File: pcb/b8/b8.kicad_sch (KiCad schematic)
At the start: 29 parts, among them J1 USB, J2 ISP Programming, SW1 SW_Push, SW2 SW_Push, SW3 SW_Push, SW4 SW_Push, SW5 SW_Push, SW6 SW_Push, SW7 SW_Push, SW8 SW_Push, U1 ATtiny4313-P, Y1 20MHz

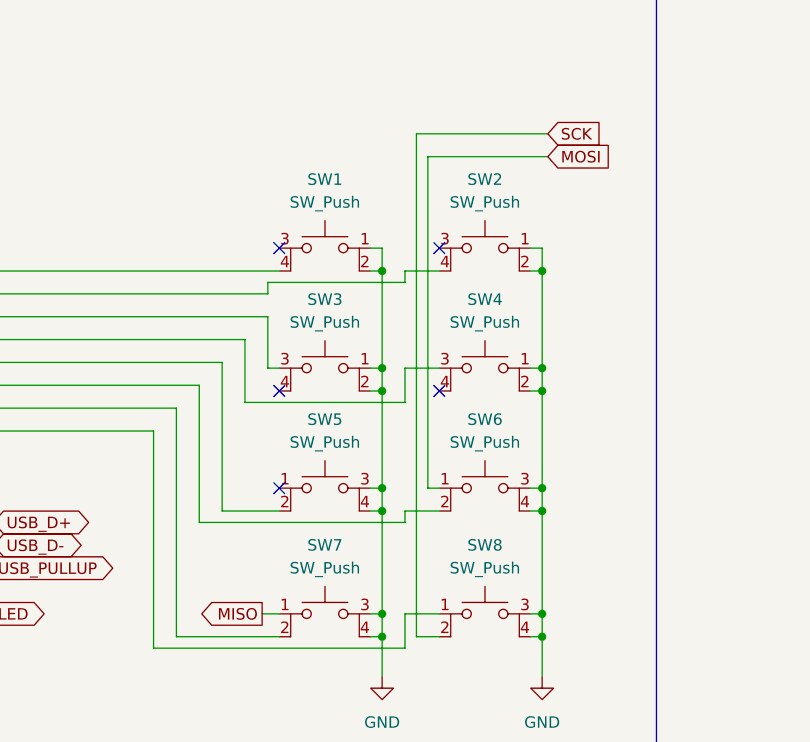
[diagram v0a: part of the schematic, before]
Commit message: pcb: b8: revision 20240403
some minor pcb fixes. this also moves the pcb files to pcb/b8, preparing
to introduce other pcb variants. this also moves the kicad library to
pcb/lib and adds the missing LICENSE file.
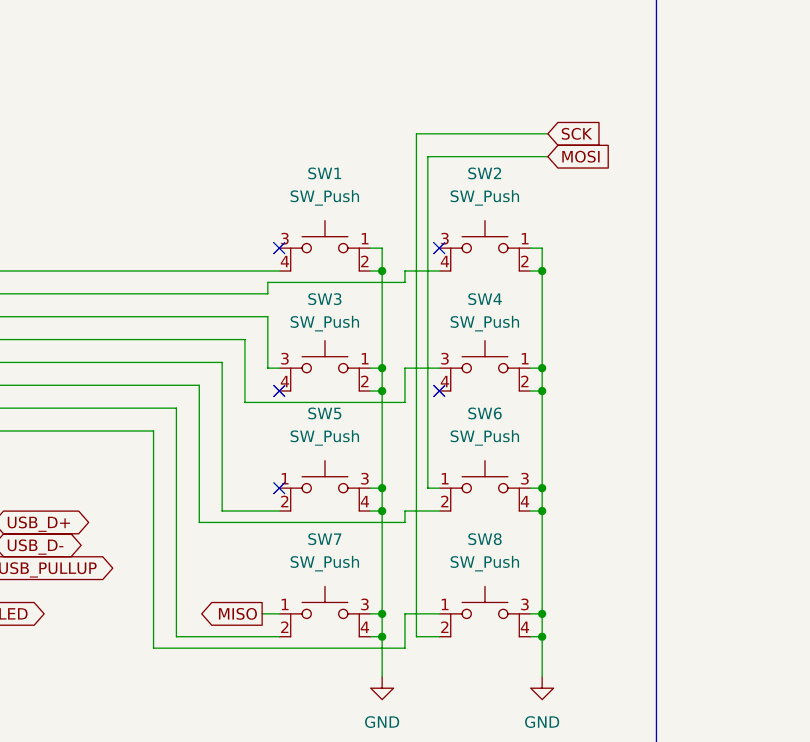
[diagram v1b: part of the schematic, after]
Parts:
- C3: footprint Capacitor_THT:C_Disc_D4.3mm_W1.9mm_P5.00mm -> b8:C_TDK_FA28
- C4: footprint custom:CP_Radial_D5.0mm_P2.50mm_Horizontal -> b8:CP_Radial_D5.0mm_P2.50mm_Horizontal
- J1: footprint custom:RND_205-00862 -> b8:USB_Mini-B_PTH
- R1, R2, R3, R4: footprint Resistor_THT:R_Axial_DIN0207_L6.3mm_D2.5mm_P10.16mm_Horizontal -> b8:R_YAGEO_MFR-25FTE52_Horizontal
- SW1, SW2, SW3, SW4, SW5, SW6, SW7, SW8: footprint custom:SW_PUSH-12mm -> b8:SW_PUSH-12mm; symbol custom:SW_Push -> b8:SW_Push
- Y1: footprint Crystal:Crystal_HC49-U_Vertical -> Crystal:Crystal_HC49-4H_Vertical
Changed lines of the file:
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@@
   (title_block
     (title "b8")
-    (date "2022-12-22")
-    (rev "1.1")
+    (date "2024-04-03")
+    (rev "20240403")
     (comment 3 "Released under CERN Open Hardware Licence Version 2 - Strongly Reciprocal")
     (comment 4 "Designed by: Rafael G. Martins")
@@
     )
   )
-  (symbol (lib_id "custom:SW_Push") (at 225.425 71.755 0) (mirror y) (unit 1)
-    (in_bom yes) (on_board yes) (dnp no) (fields_autoplaced)
-    (property "Reference" "SW2" (at 225.425 64.135 0)
-      (effects (font (size 1.27 1.27)))
-    )
-    (property "Value" "SW_Push" (at 225.425 66.675 0)
-      (effects (font (size 1.27 1.27)))
-    )
-    (property "Footprint" "custom:SW_PUSH-12mm" (at 225.425 66.675 0)
+  (symbol (lib_id "b8:SW_Push") (at 225.425 71.755 0) (mirror y) (unit 1)
+    (in_bom yes) (on_board yes) (dnp no) (fields_autoplaced)
+    (property "Reference" "SW2" (at 225.425 63.5 0)
+      (effects (font (size 1.27 1.27)))
+    )
+    (property "Value" "SW_Push" (at 225.425 66.04 0)
+      (effects (font (size 1.27 1.27)))
+    )
+    (property "Footprint" "b8:SW_PUSH-12mm" (at 225.425 66.675 0)
       (effects (font (size 1.27 1.27)) hide)
     )
@@
     )
   )
-  (symbol (lib_id "custom:SW_Push") (at 225.425 98.425 0) (unit 1)
-    (in_bom yes) (on_board yes) (dnp no) (fields_autoplaced)
-    (property "Reference" "SW6" (at 225.425 90.805 0)
-      (effects (font (size 1.27 1.27)))
-    )
-    (property "Value" "SW_Push" (at 225.425 93.345 0)
-      (effects (font (size 1.27 1.27)))
-    )
-    (property "Footprint" "custom:SW_PUSH-12mm" (at 225.425 93.345 0)
+  (symbol (lib_id "b8:SW_Push") (at 225.425 98.425 0) (unit 1)
+    (in_bom yes) (on_board yes) (dnp no) (fields_autoplaced)
+    (property "Reference" "SW6" (at 225.425 90.17 0)
+      (effects (font (size 1.27 1.27)))
+    )
+    (property "Value" "SW_Push" (at 225.425 92.71 0)
+      (effects (font (size 1.27 1.27)))
+    )
+    (property "Footprint" "b8:SW_PUSH-12mm" (at 225.425 93.345 0)
       (effects (font (size 1.27 1.27)) hide)
     )
@@
     )
   )
-  (symbol (lib_id "custom:SW_Push") (at 207.645 85.09 0) (mirror y) (unit 1)
+  (symbol (lib_id "b8:SW_Push") (at 207.645 85.09 0) (mirror y) (unit 1)
     (in_bom yes) (on_board yes) (dnp no) (fields_autoplaced)
     (property "Reference" "SW3" (at 207.645 77.47 0)
@@
       (effects (font (size 1.27 1.27)))
     )
-    (property "Footprint" "custom:SW_PUSH-12mm" (at 207.645 80.01 0)
+    (property "Footprint" "b8:SW_PUSH-12mm" (at 207.645 80.01 0)
       (effects (font (size 1.27 1.27)) hide)
     )
@@
       (effects (font (size 1.27 1.27)))
     )
-    (property "Footprint" "custom:RND_205-00862" (at 66.04 93.98 0)
+    (property "Footprint" "b8:USB_Mini-B_PTH" (at 66.04 93.98 0)
       (effects (font (size 1.27 1.27)) hide)
     )
@@
       (effects (font (size 1.27 1.27)))
     )
-    (property "Footprint" "Resistor_THT:R_Axial_DIN0207_L6.3mm_D2.5mm_P10.16mm_Horizontal" (at 87.63 97.028 90)
+    (property "Footprint" "b8:R_YAGEO_MFR-25FTE52_Horizontal" (at 87.63 97.028 90)
       (effects (font (size 1.27 1.27)) hide)
     )
@@
       (effects (font (size 1.27 1.27)))
     )
-    (property "Footprint" "custom:CP_Radial_D5.0mm_P2.50mm_Horizontal" (at 164.465 59.3598 0)
+    (property "Footprint" "b8:CP_Radial_D5.0mm_P2.50mm_Horizontal" (at 164.465 59.3598 0)
       (effects (font (size 1.27 1.27)) hide)
     )
@@
     )
   )
-  (symbol (lib_id "custom:SW_Push") (at 225.425 112.395 0) (unit 1)
-    (in_bom yes) (on_board yes) (dnp no) (fields_autoplaced)
-    (property "Reference" "SW8" (at 225.425 104.775 0)
-      (effects (font (size 1.27 1.27)))
-    )
-    (property "Value" "SW_Push" (at 225.425 107.315 0)
-      (effects (font (size 1.27 1.27)))
-    )
-    (property "Footprint" "custom:SW_PUSH-12mm" (at 225.425 107.315 0)
+  (symbol (lib_id "b8:SW_Push") (at 225.425 112.395 0) (unit 1)
+    (in_bom yes) (on_board yes) (dnp no) (fields_autoplaced)
+    (property "Reference" "SW8" (at 225.425 104.14 0)
+      (effects (font (size 1.27 1.27)))
+    )
+    (property "Value" "SW_Push" (at 225.425 106.68 0)
+      (effects (font (size 1.27 1.27)))
+    )
+    (property "Footprint" "b8:SW_PUSH-12mm" (at 225.425 107.315 0)
       (effects (font (size 1.27 1.27)) hide)
     )
@@
       (effects (font (size 1.27 1.27)))
     )
-    (property "Footprint" "Resistor_THT:R_Axial_DIN0207_L6.3mm_D2.5mm_P10.16mm_Horizontal" (at 78.105 128.143 90)
+    (property "Footprint" "b8:R_YAGEO_MFR-25FTE52_Horizontal" (at 78.105 128.143 90)
       (effects (font (size 1.27 1.27)) hide)
     )
@@
       (effects (font (size 1.27 1.27)))
     )
-    (property "Footprint" "Resistor_THT:R_Axial_DIN0207_L6.3mm_D2.5mm_P10.16mm_Horizontal" (at 87.63 94.488 90)
+    (property "Footprint" "b8:R_YAGEO_MFR-25FTE52_Horizontal" (at 87.63 94.488 90)
       (effects (font (size 1.27 1.27)) hide)
     )
@@
     )
   )
-  (symbol (lib_id "custom:SW_Push") (at 225.425 85.09 0) (mirror y) (unit 1)
+  (symbol (lib_id "b8:SW_Push") (at 225.425 85.09 0) (mirror y) (unit 1)
     (in_bom yes) (on_board yes) (dnp no) (fields_autoplaced)
     (property "Reference" "SW4" (at 225.425 77.47 0)
@@
       (effects (font (size 1.27 1.27)))
     )
-    (property "Footprint" "custom:SW_PUSH-12mm" (at 225.425 80.01 0)
+    (property "Footprint" "b8:SW_PUSH-12mm" (at 225.425 80.01 0)
       (effects (font (size 1.27 1.27)) hide)
     )
@@
     )
   )
-  (symbol (lib_id "custom:SW_Push") (at 207.645 71.755 0) (mirror y) (unit 1)
-    (in_bom yes) (on_board yes) (dnp no) (fields_autoplaced)
-    (property "Reference" "SW1" (at 207.645 64.135 0)
-      (effects (font (size 1.27 1.27)))
-    )
-    (property "Value" "SW_Push" (at 207.645 66.675 0)
-      (effects (font (size 1.27 1.27)))
-    )
-    (property "Footprint" "custom:SW_PUSH-12mm" (at 207.645 66.675 0)
+  (symbol (lib_id "b8:SW_Push") (at 207.645 71.755 0) (mirror y) (unit 1)
+    (in_bom yes) (on_board yes) (dnp no) (fields_autoplaced)
+    (property "Reference" "SW1" (at 207.645 63.5 0)
+      (effects (font (size 1.27 1.27)))
+    )
+    (property "Value" "SW_Push" (at 207.645 66.04 0)
+      (effects (font (size 1.27 1.27)))
+    )
+    (property "Footprint" "b8:SW_PUSH-12mm" (at 207.645 66.675 0)
       (effects (font (size 1.27 1.27)) hide)
     )
@@
     )
   )
-  (symbol (lib_id "custom:SW_Push") (at 207.645 98.425 0) (unit 1)
-    (in_bom yes) (on_board yes) (dnp no) (fields_autoplaced)
-    (property "Reference" "SW5" (at 207.645 90.805 0)
-      (effects (font (size 1.27 1.27)))
-    )
-    (property "Value" "SW_Push" (at 207.645 93.345 0)
-      (effects (font (size 1.27 1.27)))
-    )
-    (property "Footprint" "custom:SW_PUSH-12mm" (at 207.645 93.345 0)
+  (symbol (lib_id "b8:SW_Push") (at 207.645 98.425 0) (unit 1)
+    (in_bom yes) (on_board yes) (dnp no) (fields_autoplaced)
+    (property "Reference" "SW5" (at 207.645 90.17 0)
+      (effects (font (size 1.27 1.27)))
+    )
+    (property "Value" "SW_Push" (at 207.645 92.71 0)
+      (effects (font (size 1.27 1.27)))
+    )
+    (property "Footprint" "b8:SW_PUSH-12mm" (at 207.645 93.345 0)
       (effects (font (size 1.27 1.27)) hide)
     )
@@
       (effects (font (size 1.27 1.27)))
     )
-    (property "Footprint" "Capacitor_THT:C_Disc_D4.3mm_W1.9mm_P5.00mm" (at 151.765 59.3598 0)
+    (property "Footprint" "b8:C_TDK_FA28" (at 151.765 59.3598 0)
       (effects (font (size 1.27 1.27)) hide)
     )
@@
       (effects (font (size 1.27 1.27)) (justify right))
     )
-    (property "Footprint" "Resistor_THT:R_Axial_DIN0207_L6.3mm_D2.5mm_P10.16mm_Horizontal" (at 80.518 85.09 90)
+    (property "Footprint" "b8:R_YAGEO_MFR-25FTE52_Horizontal" (at 80.518 85.09 90)
       (effects (font (size 1.27 1.27)) hide)
     )
@@
       (effects (font (size 1.27 1.27)) (justify right))
     )
-    (property "Footprint" "Crystal:Crystal_HC49-U_Vertical" (at 126.365 84.455 0)
+    (property "Footprint" "Crystal:Crystal_HC49-4H_Vertical" (at 126.365 84.455 0)
       (effects (font (size 1.27 1.27)) hide)
     )
@@
     )
   )
-  (symbol (lib_id "custom:SW_Push") (at 207.645 112.395 0) (unit 1)
-    (in_bom yes) (on_board yes) (dnp no) (fields_autoplaced)
-    (property "Reference" "SW7" (at 207.645 104.775 0)
-      (effects (font (size 1.27 1.27)))
-    )
-    (property "Value" "SW_Push" (at 207.645 107.315 0)
-      (effects (font (size 1.27 1.27)))
-    )
-    (property "Footprint" "custom:SW_PUSH-12mm" (at 207.645 107.315 0)
-      (effects (font (size 1.27 1.27)) hide)
-    )
+  (symbol (lib_id "b8:SW_Push") (at 207.645 112.395 0) (unit 1)
+    (in_bom yes) (on_board yes) (dnp no) (fields_autoplaced)
+    (property "Reference" "SW7" (at 207.645 104.14 0)
+      (effects (font (size 1.27 1.27)))
+    )
+    (property "Value" "SW_Push" (at 207.645 106.68 0)
+      (effects (font (size 1.27 1.27)))
+    )
+    (property "Footprint" "b8:SW_PUSH-12mm" (at 207.645 107.315 0)
+      (effects (font (size 1.27 1.27)) hide)
+    )
